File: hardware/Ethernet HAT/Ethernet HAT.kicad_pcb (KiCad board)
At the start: 2 copper layers, 42 x 42 mm, 7 parts, among them J1 RJ45_Amphenol_RJMG1BD3B8K1ANR, J2 Conn_01x10_Pin, U1 W5500

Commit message: EthernetHat ordered
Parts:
- added C1: C18pF, Capacitor_SMD:C_0402_1005Metric, F.Cu at (144.6, 119.1)
- added C11: 0.1uf, Capacitor_SMD:C_0402_1005Metric, F.Cu at (142.3, 106.4)
- added C12: 0.1uf, Capacitor_SMD:C_0402_1005Metric, F.Cu at (145.3, 104.7)
- added C13: 0.1uf, Capacitor_SMD:C_0402_1005Metric, F.Cu at (140.2, 112.6)
- added C14: 10uf, Capacitor_SMD:C_0805_2012Metric, F.Cu at (141.0, 116.0)
- added C15: 0.1uf, Capacitor_SMD:C_0402_1005Metric, F.Cu at (142.8, 116.7)
- added C2: C18pF, Capacitor_SMD:C_0402_1005Metric, F.Cu at (150.4, 118.9)
- added C3: 10nF, Capacitor_SMD:C_0402_1005Metric, F.Cu at (149.6, 103.2)
- added C4: 22nF, Capacitor_SMD:C_0402_1005Metric, F.Cu at (158.0, 103.2)
- added C5: 4.7uf, Capacitor_SMD:C_0402_1005Metric, F.Cu at (140.2, 111.5)
- added C6: 10nf, Capacitor_SMD:C_0402_1005Metric, F.Cu at (140.2, 113.7)
- added C7: 10uf, Capacitor_SMD:C_0805_2012Metric, F.Cu at (139.8, 108.3)
- added C8: 0.1uf, Capacitor_SMD:C_0402_1005Metric, F.Cu at (140.2, 110.1)
- added D1: LED, LED_SMD:LED_0603_1608Metric, F.Cu at (142.0, 81.0)
- added D2: LED, LED_SMD:LED_0603_1608Metric, F.Cu at (139.8, 81.0)
- added L1: 10uH, Inductor_SMD:L_0603_1608Metric, F.Cu at (140.0, 106.3)
- added R1: R1M, Resistor_SMD:R_0402_1005Metric, F.Cu at (147.0, 116.5)
- added R10: 330, Resistor_SMD:R_0402_1005Metric, F.Cu at (141.0, 86.4)
- added R11: 330, Resistor_SMD:R_0402_1005Metric, F.Cu at (141.0, 87.8)
- added R12: 10, Resistor_SMD:R_0402_1005Metric, F.Cu at (156.6, 103.2)
- added R13: 330, Resistor_SMD:R_0402_1005Metric, F.Cu at (141.0, 83.6)
- added R14: 330, Resistor_SMD:R_0402_1005Metric, F.Cu at (141.0, 85.0)
- added R15: 10, Resistor_SMD:R_0402_1005Metric, F.Cu at (148.2, 103.2)
- added R16: 49.9, Resistor_SMD:R_0402_1005Metric, F.Cu at (146.8, 103.2)
- added R17: 49.9, Resistor_SMD:R_0402_1005Metric, F.Cu at (151.0, 103.2)
- added R2: 33, Resistor_SMD:R_0402_1005Metric, F.Cu at (153.8, 103.2)
- added R3: 33, Resistor_SMD:R_0402_1005Metric, F.Cu at (159.4, 103.2)
- added R4: 33, Resistor_SMD:R_0402_1005Metric, F.Cu at (145.4, 103.2)
- added R5: 33, Resistor_SMD:R_0402_1005Metric, F.Cu at (152.4, 103.2)
- added R6: 49.9, Resistor_SMD:R_0402_1005Metric, F.Cu at (160.8, 103.2)
- added R7: 49.9, Resistor_SMD:R_0402_1005Metric, F.Cu at (155.2, 103.2)
- added R8: 12.4k, Resistor_SMD:R_0402_1005Metric, F.Cu at (142.6, 103.2)
- added Y1: Crystal_25MHz, Crystal:Crystal_SMD_3225-4Pin_3.2x2.5mm, F.Cu at (147.4, 118.9)
- H1, H2, H3, H4: footprint MountingHole:MountingHole_3.2mm_M3 -> MountingHole:MountingHole_3.2mm_M3_ISO14580_Pad
- J2: value Conn_01x10_Pin -> 1-84952-4; footprint Connector_PinHeader_2.54mm:PinHeader_2x05_P2.54mm_Vertical -> Connector_FFC-FPC:TE_1-84952-4_1x14-1MP_P1.0mm_Horizontal
- moved H1 43.8 mm to (134.5, 84.5)
- moved H2 31.0 mm to (165.5, 115.5)
- moved H3 31.0 mm to (134.5, 115.5)
- moved U1 12.5 mm to (147.0, 110.6), turned to -90 degrees
- moved J2 10.4 mm to (166.2, 100.0), turned to 90 degrees
- moved J1 5.94 mm to (157.7, 96.3)
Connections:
- net Net-(U1-AVDD-Pad11) renamed 3V3A
- J1 pad L1: unconnected-(J1-LEDY_A-PadL1) -> +3.3V
- J1 pad L2: unconnected-(J1-LEDY_K-PadL2) -> Net-(J1-LEDY_K)
- J1 pad L3: unconnected-(J1-LEDG_K-PadL3) -> Net-(J1-LEDG_K)
- J1 pad L4: unconnected-(J1-LEDG_A-PadL4) -> +3.3V
- J1 pad R1: unconnected-(J1-TD+-PadR1) -> Net-(J1-TD+)
- J1 pad R2: unconnected-(J1-TD--PadR2) -> Net-(J1-TD-)
- J1 pad R3: unconnected-(J1-RD+-PadR3) -> Net-(J1-RD+)
- J1 pad R4: unconnected-(J1-TCT-PadR4) -> TCT
- J1 pad R5: unconnected-(J1-RCT-PadR5) -> RCT
- J1 pad R6: unconnected-(J1-RD--PadR6) -> Net-(J1-RD-)
- J1 pad R8: unconnected-(J1-GND-PadR8) -> GND
- J1 pad SH: unconnected-(J1-SHIELD-PadSH) -> GND
- J2 pad 1: unconnected-(J2-Pin_1-Pad1) -> GND
- J2 pad 10: unconnected-(J2-Pin_10-Pad10) -> AUX5
- J2 pad 2: unconnected-(J2-Pin_2-Pad2) -> AUX1
- J2 pad 3: unconnected-(J2-Pin_3-Pad3) -> AUX2
- J2 pad 4: unconnected-(J2-Pin_4-Pad4) -> MISO
- J2 pad 5: unconnected-(J2-Pin_5-Pad5) -> ETH_CS
- J2 pad 6: unconnected-(J2-Pin_6-Pad6) -> MOSI
- J2 pad 7: unconnected-(J2-Pin_7-Pad7) -> SCK
- J2 pad 8: unconnected-(J2-Pin_8-Pad8) -> AUX3
- J2 pad 9: unconnected-(J2-Pin_9-Pad9) -> AUX4
- U1 pad 1: unconnected-(U1-TXN-Pad1) -> Net-(U1-TXN)
- U1 pad 10: unconnected-(U1-EXRES1-Pad10) -> Net-(U1-EXRES1)
- U1 pad 14: Net-(U1-AGND-Pad14) -> GND
- U1 pad 16: Net-(U1-AGND-Pad14) -> GND
- U1 pad 19: Net-(U1-AGND-Pad14) -> GND
- U1 pad 2: unconnected-(U1-TXP-Pad2) -> Net-(U1-TXP)
- U1 pad 20: unconnected-(U1-TOCAP-Pad20) -> Net-(U1-TOCAP)
- U1 pad 22: unconnected-(U1-1V2O-Pad22) -> Net-(U1-1V2O)
- U1 pad 24: unconnected-(U1-SPDLED-Pad24) -> Net-(U1-SPDLED)
- U1 pad 25: unconnected-(U1-LINKLED-Pad25) -> Net-(U1-LINKLED)
- U1 pad 26: unconnected-(U1-DUPLED-Pad26) -> Net-(U1-DUPLED)
- U1 pad 27: unconnected-(U1-ACTLED-Pad27) -> Net-(U1-ACTLED)
- U1 pad 28: unconnected-(U1-VDD-Pad28) -> +3.3V
- U1 pad 29: unconnected-(U1-GND-Pad29) -> GND
- U1 pad 3: Net-(U1-AGND-Pad14) -> GND
- U1 pad 30: unconnected-(U1-XI/CLKIN-Pad30) -> Net-(U1-XI/CLKIN)
- U1 pad 31: unconnected-(U1-XO-Pad31) -> Net-(U1-XO)
- U1 pad 32: unconnected-(U1-~{SCS}-Pad32) -> ETH_CS
- U1 pad 33: unconnected-(U1-SCLK-Pad33) -> SCK
- U1 pad 34: unconnected-(U1-MISO-Pad34) -> MISO
- U1 pad 35: unconnected-(U1-MOSI-Pad35) -> MOSI
- U1 pad 36: unconnected-(U1-~{INT}-Pad36) -> AUX4
- U1 pad 37: unconnected-(U1-~{RST}-Pad37) -> AUX6
- U1 pad 43: unconnected-(U1-PMODE2-Pad43) -> AUX5
- U1 pad 44: unconnected-(U1-PMODE1-Pad44) -> AUX1
- U1 pad 45: unconnected-(U1-PMODE0-Pad45) -> AUX2
- U1 pad 48: Net-(U1-AGND-Pad14) -> GND
- U1 pad 5: unconnected-(U1-RXN-Pad5) -> Net-(U1-RXN)
- U1 pad 6: unconnected-(U1-RXP-Pad6) -> Net-(U1-RXP)
- U1 pad 9: Net-(U1-AGND-Pad14) -> GND
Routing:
- net GND: track 0.00 -> 54.5 mm, vias 0 -> 11
- net 3V3A: track 0.00 -> 42.6 mm, vias 0 -> 4
- net Net-(U1-DUPLED): track 0.00 -> 37.5 mm, vias 0 -> 2
- net Net-(U1-SPDLED): track 0.00 -> 33.1 mm, vias 0 -> 2
- net Net-(U1-LINKLED): track 0.00 -> 32.1 mm, vias 0 -> 2
- net Net-(U1-ACTLED): track 0.00 -> 31.0 mm, vias 0 -> 2
- net SCK: track 0.00 -> 28.0 mm
- net ETH_CS: track 0.00 -> 27.9 mm
- net AUX6: track 0.00 -> 26.5 mm, vias 0 -> 2
- net MOSI: track 0.00 -> 25.8 mm, vias 0 -> 2
- net MISO: track 0.00 -> 25.7 mm, vias 0 -> 2
- net AUX4: track 0.00 -> 25.1 mm
- net AUX5: track 0.00 -> 22.7 mm, vias 0 -> 2
- net AUX1: track 0.00 -> 21.7 mm, vias 0 -> 2
- net AUX2: track 0.00 -> 21.6 mm, vias 0 -> 2
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- added copper zone on In2.Cu, net +3.3V
- added copper zone on In2.Cu, net 3V3A
- added copper zone on In1.Cu, net GND
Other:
- copper layers 2 -> 4
- board text added: "DPX"
- board text added: "Ethernet HAT"
- board text added: "JLCJLCJLCJLC"
- board text added: "SPD"
- board text added: "V1.0.0"

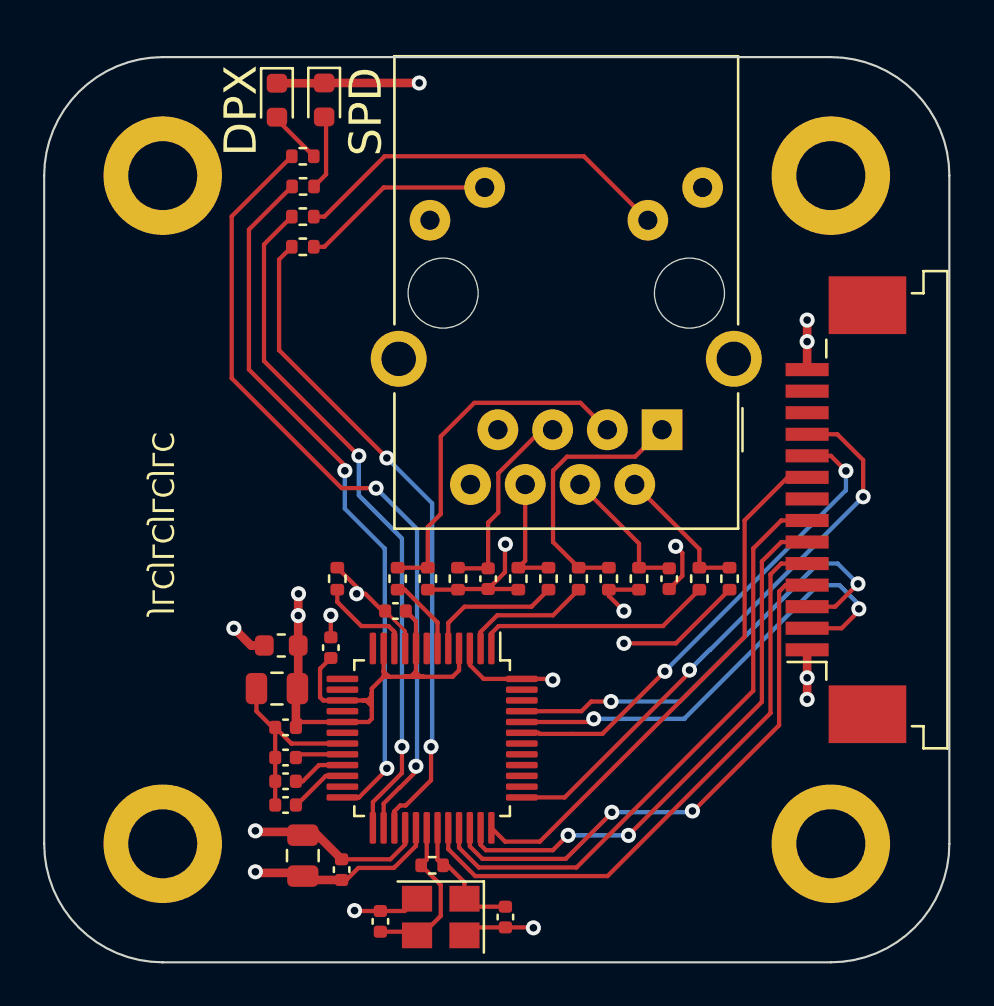
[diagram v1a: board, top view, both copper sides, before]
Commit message: EthernetHat V1.2.0 ordered
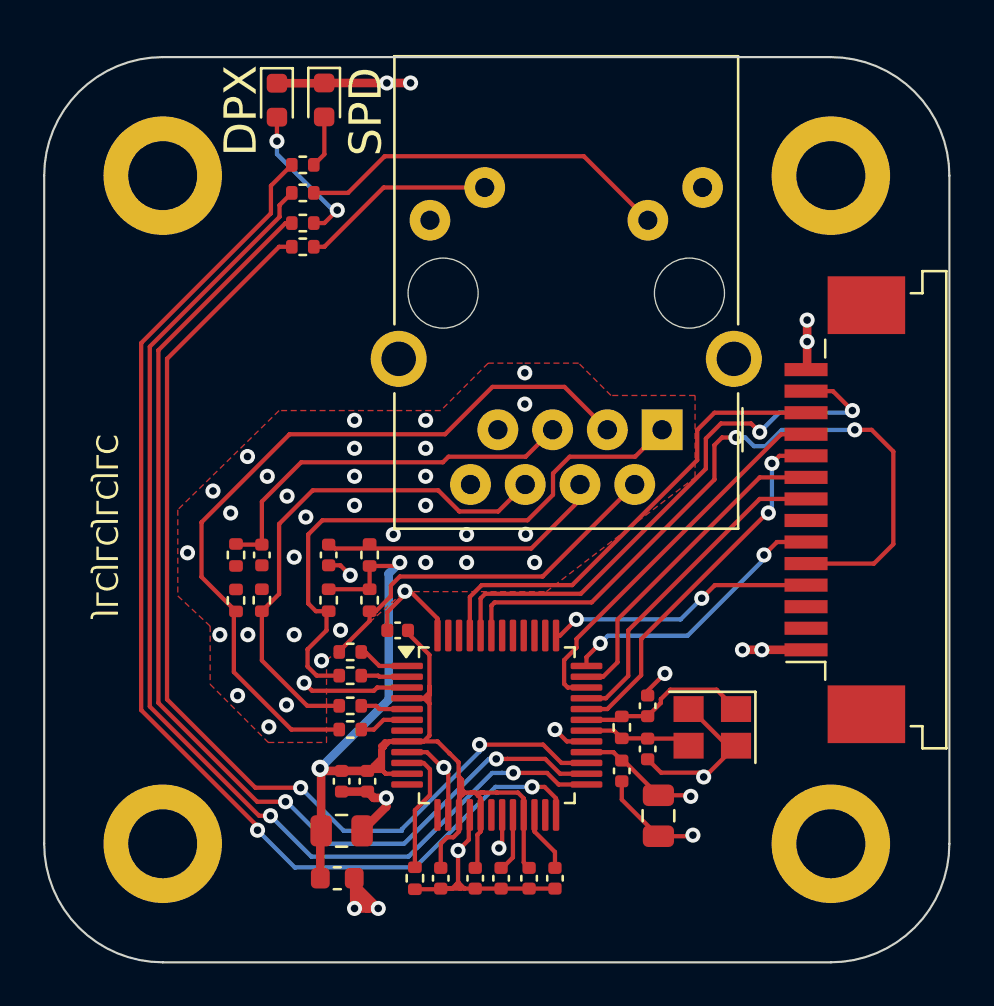
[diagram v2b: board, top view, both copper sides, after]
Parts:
- added C10: 0.1uf, Capacitor_SMD:C_0402_1005Metric, F.Cu at (145.4, 105.6)
- added C9: 0.1uf, Capacitor_SMD:C_0402_1005Metric, F.Cu at (149.0, 117.1)
- moved R6 16.7 mm to (144.1, 104.2), turned to -90 degrees
- moved C14 16.6 mm to (157.5, 114.2)
- moved R3 16.6 mm to (143.2, 106.6), turned to 180 degrees
- moved C4 15.8 mm to (142.2, 102.1)
- moved Y1 15.4 mm to (160.0, 110.1)
- moved C1 14.8 mm to (157.0, 111.1), turned to 90 degrees
- moved R8 14.4 mm to (146.2, 117.1), turned to -90 degrees
- moved C15 13.8 mm to (155.8, 112.1)
- moved R7 13.0 mm to (142.2, 104.2), turned to -90 degrees
- moved C6 13.0 mm to (152.7, 117.1), turned to -90 degrees
- moved R12 12.5 mm to (144.1, 102.1)
- moved C13 12.2 mm to (151.5, 117.1), turned to -90 degrees
- moved R17 11.9 mm to (139.1, 104.2), turned to -90 degrees
- moved C2 11.8 mm to (157.0, 109.1), turned to 90 degrees
- moved R2 11.5 mm to (143.2, 107.7), turned to 180 degrees
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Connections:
- net Net-(J1-RD+) renamed /RD+
- net Net-(J1-RD-) renamed /RD-
- net Net-(J1-TD+) renamed /TD+
- net Net-(J1-TD-) renamed /TD-
- J2 pad 1: GND -> +3.3V
- J2 pad 10: AUX5 -> ETH_CS
- J2 pad 11: AUX6 -> MISO
- J2 pad 12: SCL1 -> AUX2
- J2 pad 13: SDA1 -> AUX1
- J2 pad 14: +3.3V -> GND
- J2 pad 2: AUX1 -> SDA1
- J2 pad 3: AUX2 -> SCL1
- J2 pad 4: MISO -> AUX6
- J2 pad 5: ETH_CS -> AUX5
- J2 pad 6: MOSI -> AUX4
- J2 pad 7: SCK -> AUX3
- J2 pad 8: AUX3 -> SCK
- J2 pad 9: AUX4 -> MOSI
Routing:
- net Net-(U1-SPDLED): track 33.1 -> 53.1 mm
- net 3V3A: track 42.6 -> 62.6 mm, vias 4 -> 2
- net Net-(U1-LINKLED): track 32.1 -> 51.5 mm
- net /RD+: track 16.6 -> 35.9 mm
- net /RD-: track 5.39 -> 24.1 mm
- net Net-(U1-ACTLED): track 31.0 -> 48.0 mm
- net /TD+: track 12.2 -> 27.9 mm
- net AUX6: track 26.5 -> 12.6 mm
- net SCK: track 28.0 -> 15.3 mm
- net AUX4: track 25.1 -> 12.9 mm, vias 0 -> 2
- net Net-(U1-DUPLED): track 37.5 -> 49.5 mm
- net AUX5: track 22.7 -> 33.8 mm
- net /TD-: track 6.50 -> 17.5 mm
- net ETH_CS: track 27.9 -> 17.3 mm, vias 0 -> 2
- net MOSI: track 25.8 -> 15.2 mm, vias 2 -> 0
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- added copper zone on F.Cu, net GND
- removed copper zone on In2.Cu, net 3V3A
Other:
- board text added: "V1.1.0"
- board text removed: "V1.0.0"

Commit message: Ethernet HAT V1.2.0
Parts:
- removed R15: 10, Resistor_SMD:R_0402_1005Metric
- added C16: 6.8n, Capacitor_SMD:C_0402_1005Metric, F.Cu at (137.5, 102.1)
- added C17: 6.8n, Capacitor_SMD:C_0402_1005Metric, F.Cu at (138.5, 102.1)
- added J3: Debug Connector, GE_Connector:Conn_01x14_Flat2.54, B.Cu at (169.6, 83.4)
- R8: footprint Resistor_SMD:R_0402_1005Metric -> Resistor_SMD:R_0603_1608Metric
- moved R4 3.60 mm to (143.2, 106.6)
- moved R12 3.05 mm to (142.1, 99.8)
- moved C4 2.59 mm to (141.0, 99.8)
- moved R2 1.40 mm to (143.2, 109.1)
- moved R3 1.10 mm to (143.2, 107.7)
- moved R5 1.10 mm to (143.2, 110.2)
- moved R16 1.09 mm to (137.0, 103.6), turned to 180 degrees
- moved R7 0.98 mm to (141.3, 103.8), turned to 0 degrees
- moved R6 0.89 mm to (143.3, 103.8), turned to 180 degrees
- moved R8 0.72 mm to (145.8, 117.7)
- moved R17 0.61 mm to (139.0, 103.6), turned to 0 degrees
- moved C3 0.40 mm to (139.5, 102.1), turned to 90 degrees
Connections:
- net Net-(J1-LEDG_K) renamed /LK_LED
- net Net-(J1-LEDY_K) renamed /ACT_LED
- J1 pad R3: /RD+ -> /R+
- J1 pad R6: /RD- -> /R-
- R16 pad 1: GND -> /RD+
- R16 pad 2: /RD+ -> RCT
- R17 pad 1: GND -> /RD-
- R17 pad 2: /RD- -> RCT
- R2 pad 1: Net-(U1-TXP) -> Net-(U1-RXN)
- R2 pad 2: /TD+ -> /RD-
- R3 pad 1: Net-(U1-TXN) -> Net-(U1-TXP)
- R3 pad 2: /TD- -> /TD+
- R4 pad 1: Net-(U1-RXP) -> Net-(U1-TXN)
- R4 pad 2: /RD+ -> /TD-
- R5 pad 1: Net-(U1-RXN) -> Net-(U1-RXP)
- R5 pad 2: /RD- -> /RD+
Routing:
- net /R-: track 0.00 -> 25.7 mm
- net /R+: track 0.00 -> 25.7 mm
- net /RD+: track 35.9 -> 10.3 mm
- net /RD-: track 24.1 -> 10.3 mm
- net SDA1: track 0.00 -> 11.8 mm, vias 0 -> 1
- net SCL1: track 0.00 -> 10.2 mm, vias 0 -> 1
- net +3.3V: track 14.1 -> 24.2 mm, vias 5 -> 8
- net ETH_CS: track 17.3 -> 26.8 mm
- net AUX2: track 21.7 -> 31.1 mm, vias 0 -> 1
- net GND: track 57.4 -> 66.6 mm, vias 47 -> 28
- net AUX6: track 12.6 -> 21.5 mm, vias 2 -> 3
- net MISO: track 18.0 -> 26.9 mm, vias 0 -> 1
- net AUX4: track 12.9 -> 19.6 mm, vias 2 -> 3
- net RCT: track 18.1 -> 24.7 mm, vias 0 -> 2
- net AUX1: track 26.3 -> 32.7 mm, vias 2 -> 3
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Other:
- board text added: "V1.2.0"
- board text removed: "V1.1.0"
